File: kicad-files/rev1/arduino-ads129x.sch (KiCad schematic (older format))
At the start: 163 parts

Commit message: added 32kHz and 12MHz clock crystals
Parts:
- added C? (x4): 20pF, symbol C
- added X?: 12MHz 20pF, symbol CRYSTAL
- added X?: 32.768KHz 1.2pF, symbol CRYSTAL
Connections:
- wire segments 773 -> 608

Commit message: connected USB to SAM3X
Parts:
- added C?: 20pF, symbol C
- added R? (x2): 39, symbol R
- added R?: 6.8k, symbol R
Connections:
- wire segments 608 -> 814
- no-connect marks 1 -> 3
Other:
- note added: "See SAM3X data sheet section 40.5.1.9 Plug-In Detection:\nIn device mode, USB is detected when VBUS >= 1.4V"
- note added: "UOTGVBOF not needed; won't power VBUS\n"
- note added: "USB OTG ID not connected is slave"

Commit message: added fuse and zener on isolated side
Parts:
- added D?: ZENER, symbol ZENER
- added TH?: PTC, symbol THERMISTOR
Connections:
- wire segments 814 -> 624

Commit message: added power indicator LED to isolated 3.3V
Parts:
- added D?: LED, symbol LED
- added R?: 1k, symbol R
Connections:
- wire segments 624 -> 627
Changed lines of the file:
@@
-EESchema Schematic File Version 2  date Sat 18 May 2013 12:56:10 PM CEST
+EESchema Schematic File Version 2  date Sat 18 May 2013 01:12:58 PM CEST
 LIBS:power
 LIBS:device
@@
 $EndDescr
 Wire Wire Line
+	25700 4750 25700 4950
+Wire Wire Line
 	32850 2450 33000 2450
 Wire Wire Line
-	19250 16900 19250 17900
+	19250 17900 19250 16900
 Connection ~ 18950 17650
 Wire Wire Line
@@
 	20150 18450 20150 18400
 Wire Wire Line
-	20500 18450 20500 18500
+	20500 18500 20500 18450
 Connection ~ 20750 17700
 Connection ~ 17200 15900
@@
 	36150 5200 36050 5200
 Wire Wire Line
-	35600 4400 36150 4400
+	36150 4400 35600 4400
 Wire Wire Line
 	36150 4000 35950 4000
@@
 	33400 2450 33700 2450
 Wire Wire Line
-	35300 2450 35900 2450
+	35900 2450 35300 2450
 Wire Wire Line
 	34500 2600 34500 2450
@@
 	37300 1700 37300 750
 Wire Wire Line
-	38700 2450 39550 2450
+	39550 2450 38700 2450
 Connection ~ 39100 2450
 Connection ~ 35500 2450
@@
 	38800 2900 38800 3100
 Wire Wire Line
-	38100 2450 38000 2450
+	38000 2450 38100 2450
 Wire Wire Line
 	38000 3100 38000 2650
@@
 Connection ~ 18100 5450
 Wire Wire Line
-	20050 5450 18100 5450
-Wire Wire Line
-	18100 5550 18100 5400
+	18100 5450 20050 5450
+Wire Wire Line
+	18100 5400 18100 5550
 Connection ~ 17950 6600
 Wire Wire Line
@@
 Connection ~ 21300 7350
 Wire Wire Line
-	21650 7350 20900 7350
-Wire Wire Line
-	20900 7450 20900 7300
+	20900 7350 21650 7350
+Wire Wire Line
+	20900 7300 20900 7450
 Wire Wire Line
 	21300 7450 21300 7350
@@
 	20100 7350 20100 7450
 Wire Wire Line
-	18500 7450 18500 6600
+	18500 6600 18500 7450
 Connection ~ 16600 6100
 Wire Wire Line
@@
 Connection ~ 17000 5450
 Wire Wire Line
-	17350 5450 16600 5450
+	16600 5450 17350 5450
 Wire Wire Line
 	22000 4700 22000 4800
@@
 	22400 5550 22400 5450
 Wire Wire Line
-	22000 5550 22000 5400
-Wire Wire Line
-	20900 5550 20900 5400
+	22000 5400 22000 5550
+Wire Wire Line
+	20900 5400 20900 5550
 Wire Wire Line
 	21300 5550 21300 5450
@@
 	10900 1200 10900 2600
 Wire Wire Line
-	15250 2050 13950 2050
+	13950 2050 15250 2050
 Connection ~ 15350 800
 Wire Wire Line
@@
 	10800 1900 10800 2600
 Wire Wire Line
-	12550 4550 12550 5250
+	12550 5250 12550 4550
 Connection ~ 13950 800
 Wire Wire Line
@@
 	700  950  700  900
 Wire Wire Line
-	1250 1000 1250 850
-Wire Wire Line
-	1000 1000 1000 850
+	1250 850  1250 1000
+Wire Wire Line
+	1000 850  1000 1000
 Wire Wire Line
 	2950 4200 3000 4200
@@
 	5350 6950 5350 6750
 Wire Wire Line
-	5600 6750 5150 6750
+	5150 6750 5600 6750
 Wire Wire Line
 	5750 6950 5950 6950
@@
 	5950 6500 5750 6500
 Wire Wire Line
-	5600 6300 5150 6300
+	5150 6300 5600 6300
 Wire Wire Line
 	5350 6500 5350 6300
@@
 	5350 5600 5350 5400
 Wire Wire Line
-	5150 5400 5600 5400
+	5600 5400 5150 5400
 Wire Wire Line
 	5750 5600 5950 5600
@@
 	5950 6050 5750 6050
 Wire Wire Line
-	5150 5850 5600 5850
+	5600 5850 5150 5850
 Wire Wire Line
 	5350 6050 5350 5850
@@
 	5350 7850 5350 7650
 Wire Wire Line
-	5600 7650 5150 7650
+	5150 7650 5600 7650
 Wire Wire Line
 	5750 7850 5950 7850
@@
 	5950 7400 5750 7400
 Wire Wire Line
-	5600 7200 5150 7200
+	5150 7200 5600 7200
 Wire Wire Line
 	5350 7400 5350 7200
@@
 	5350 8300 5350 8100
 Wire Wire Line
-	5150 8100 5600 8100
+	5600 8100 5150 8100
 Wire Wire Line
 	5750 8300 5950 8300
@@
 	5950 8750 5750 8750
 Wire Wire Line
-	5150 8550 5600 8550
+	5600 8550 5150 8550
 Wire Wire Line
 	5350 8750 5350 8550
@@
 	5350 5150 5350 4950
 Wire Wire Line
-	5600 4950 5150 4950
+	5150 4950 5600 4950
 Wire Wire Line
 	5750 5150 5950 5150
@@
 	5950 4700 5750 4700
 Wire Wire Line
-	5600 4500 5150 4500
+	5150 4500 5600 4500
 Wire Wire Line
 	5350 4700 5350 4500
@@
 	5350 3800 5350 3600
 Wire Wire Line
-	5150 3600 5600 3600
+	5600 3600 5150 3600
 Wire Wire Line
 	5750 3800 5950 3800
@@
 	5950 4250 5750 4250
 Wire Wire Line
-	5150 4050 5600 4050
+	5600 4050 5150 4050
 Wire Wire Line
 	5350 4250 5350 4050
@@
 	5350 2450 5350 2250
 Wire Wire Line
-	5600 2250 5150 2250
+	5150 2250 5600 2250
 Wire Wire Line
 	5750 2450 5950 2450
@@
 	5950 2000 5750 2000
 Wire Wire Line
-	5600 1800 5150 1800
+	5150 1800 5600 1800
 Wire Wire Line
 	5350 2000 5350 1800
@@
 	5350 2900 5350 2700
 Wire Wire Line
-	5150 2700 5600 2700
+	5600 2700 5150 2700
 Wire Wire Line
 	5750 2900 5950 2900
@@
 	5950 3350 5750 3350
 Wire Wire Line
-	5150 3150 5600 3150
+	5600 3150 5150 3150
 Wire Wire Line
 	9600 4450 9500 4450
@@
 	2350 4350 2350 4300
 Wire Wire Line
-	1000 1150 1000 1400
-Wire Wire Line
-	1250 1150 1250 1400
+	1000 1400 1000 1150
+Wire Wire Line
+	1250 1400 1250 1150
 Wire Wire Line
 	1550 900  1550 950
@@
 Connection ~ 19300 5450
 Wire Wire Line
-	16600 5550 16600 5400
-Wire Wire Line
-	20900 5450 21750 5450
+	16600 5400 16600 5550
+Wire Wire Line
+	21750 5450 20900 5450
 Connection ~ 21300 5450
 Wire Wire Line
-	22000 5450 22750 5450
+	22750 5450 22000 5450
 Connection ~ 22400 5450
 Wire Wire Line
@@
 Connection ~ 18900 7350
 Wire Wire Line
-	18500 7350 20500 7350
+	20500 7350 18500 7350
 Connection ~ 18500 6600
 Wire Wire Line
@@
 	42900 2200 42900 2550
 Wire Wire Line
-	43250 3300 43250 2950
+	43250 2950 43250 3300
 Connection ~ 43250 3100
 Wire Wire Line
-	41950 2450 39750 2450
+	39750 2450 41950 2450
 Wire Wire Line
 	43250 2400 44000 2400
@@
 Connection ~ 26700 2450
 Wire Wire Line
-	26700 2500 26700 2400
+	26700 2400 26700 2500
 Connection ~ 27050 1850
 Wire Wire Line
@@
 Connection ~ 29200 2350
 Wire Wire Line
-	29750 2350 28550 2350
+	28550 2350 29750 2350
 Wire Wire Line
 	28850 2600 28850 2550
@@
 Connection ~ 26700 1850
 Wire Wire Line
-	26700 2450 27250 2450
+	27250 2450 26700 2450
 Wire Wire Line
 	27050 2350 27050 2450
@@
 Connection ~ 26700 5550
 Wire Wire Line
-	26250 4750 26250 5550
-Wire Wire Line
-	26250 5550 29750 5550
+	26250 5550 26250 4750
 Connection ~ 27050 4900
 Wire Wire Line
 	27050 4800 27050 4900
 Wire Wire Line
-	27250 4900 26700 4900
+	26700 4900 27250 4900
 Connection ~ 26700 4300
 Wire Wire Line
@@
 	28850 5000 28850 5050
 Wire Wire Line
-	28550 4800 29750 4800
+	29750 4800 28550 4800
 Connection ~ 29200 4800
 Wire Wire Line
@@
 Connection ~ 27050 4300
 Wire Wire Line
-	26700 4850 26700 4950
+	26700 4950 26700 4850
 Connection ~ 26700 4900
 Wire Wire Line
@@
 Connection ~ 41750 2450
 Wire Wire Line
-	38400 4400 39000 4400
+	39000 4400 38400 4400
 Wire Wire Line
 	38650 4800 38400 4800
@@
 Connection ~ 23350 5450
 Wire Wire Line
-	23700 5450 22950 5450
-Wire Wire Line
-	22950 5550 22950 5400
+	22950 5450 23700 5450
+Wire Wire Line
+	22950 5400 22950 5550
 Wire Wire Line
 	23350 5550 23350 5450
@@
 Connection ~ 16950 16650
 Wire Wire Line
-	20150 18000 20150 16250
+	20150 16250 20150 18000
 Wire Wire Line
 	19400 16400 19400 16250
@@
 Connection ~ 19400 17150
 Wire Wire Line
-	18950 18400 18950 18150
+	18950 18150 18950 18400
 Wire Wire Line
 	18700 18200 18700 18250
@@
 Connection ~ 18950 18250
 Wire Wire Line
-	19400 16900 19400 17900
-Wire Wire Line
-	18950 17750 18950 16250
+	19400 17900 19400 16900
+Wire Wire Line
+	18950 16250 18950 17750
 Wire Wire Line
 	33700 2850 31550 2850
 Connection ~ 32200 2850
 Wire Wire Line
-	32350 2450 31550 2450
+	31550 2450 32350 2450
 Connection ~ 32200 2450
+Wire Wire Line
+	25700 4300 25700 4350
+Connection ~ 25700 4300
+Wire Wire Line
+	25700 5450 25700 5550
+Wire Wire Line
+	25700 5550 29750 5550
+Connection ~ 26250 5550
+$Comp
+L R R?
+U 1 1 51976086
+P 25700 5200
+F 0 "R?" V 25780 5200 50  0000 C CNN
+F 1 "1k" V 25700 5200 50  0000 C CNN
+	1    25700 5200
+	1    0    0    -1
+$EndComp
+$Comp
+L LED D?
+U 1 1 51976061
+P 25700 4550
+F 0 "D?" H 25700 4650 50  0000 C CNN
+F 1 "LED" H 25700 4450 50  0000 C CNN
+	1    25700 4550
+	0    1    1    0
+$EndComp
 $Comp
 L ZENER D?

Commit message: added reset button
A capacitor is not strictly required, but the data sheet
recommends a 10nF capacitor in harsh environments.

We chose a 100nF capacitor to keep the parts list and
assembly instructions simple.
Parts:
- added C?: 100nF, symbol C
- added SW?: SW_PUSH, symbol SW_PUSH
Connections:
- net labels added: RESET
- wire segments 627 -> 633
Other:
- note added: "Data sheet\nspec is\n10nF"

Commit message: added JTAG
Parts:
- added P?: JTAG, symbol CONN_5X2
- added R? (x4): 100k, symbol R
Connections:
- net labels added: JTAG_RESET, JTAG_TCK, JTAG_TDI, JTAG_TDO, JTAG_TMS
- wire segments 633 -> 659
- no-connect marks 3 -> 4

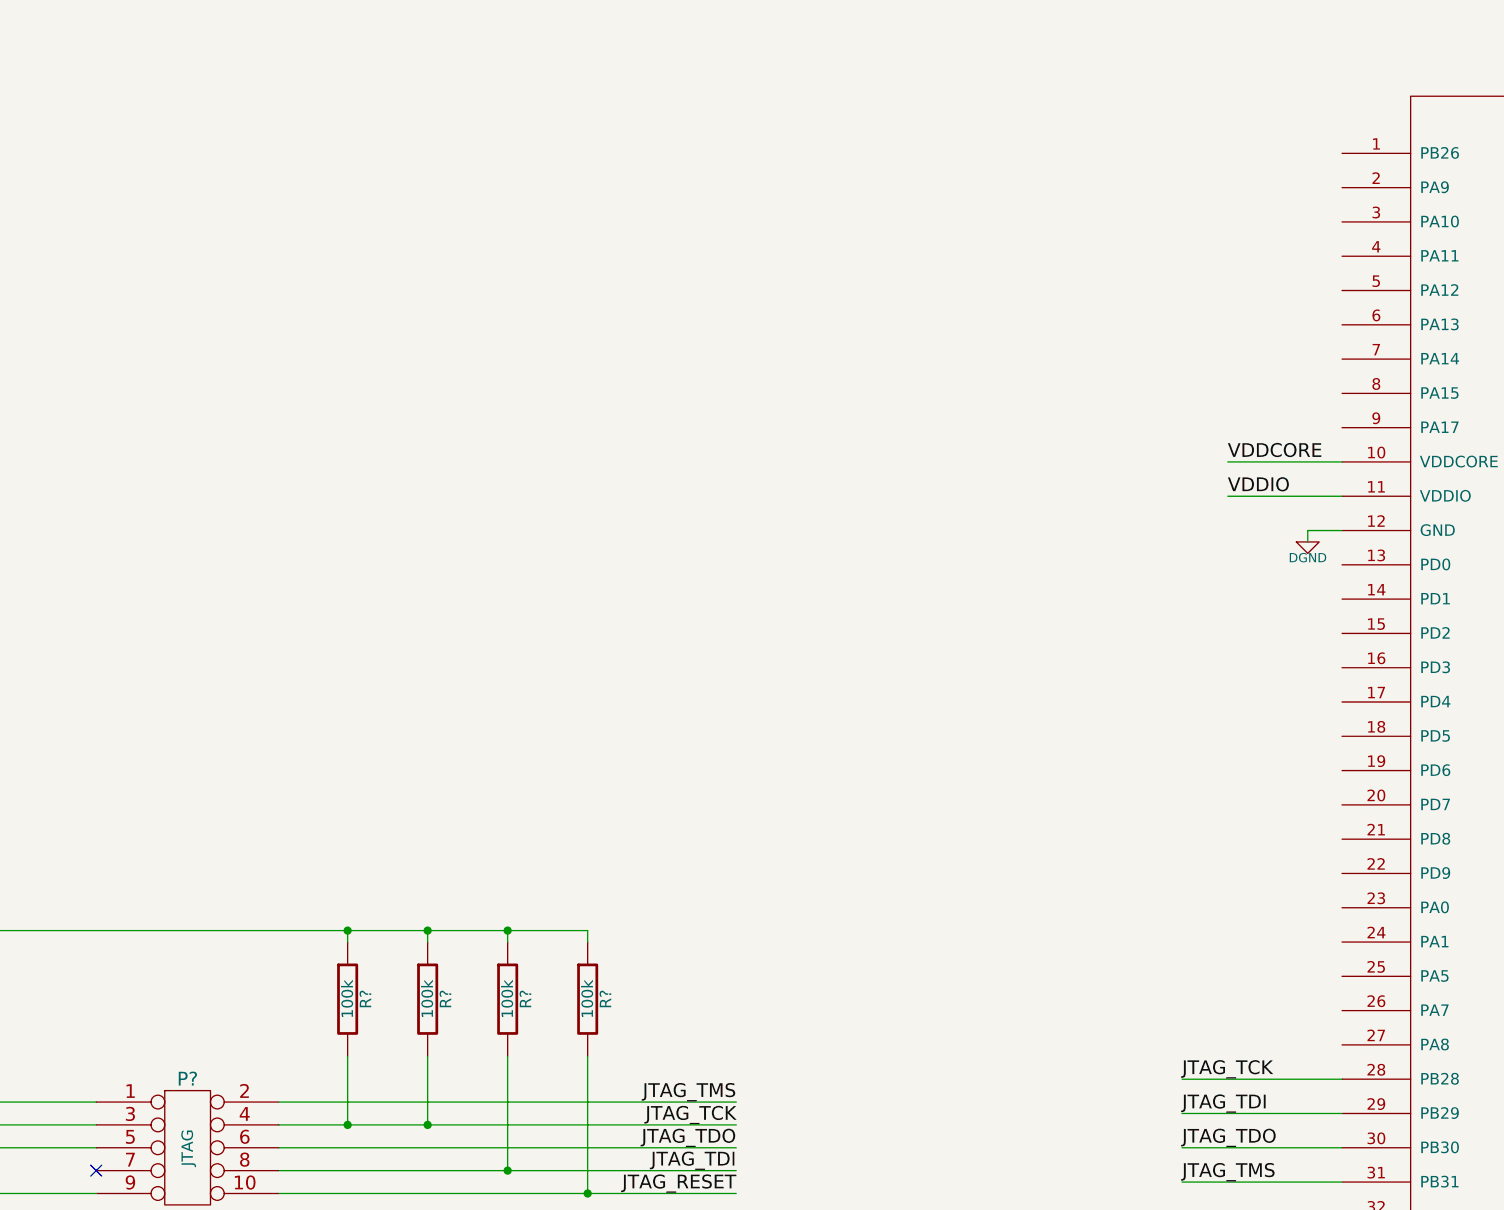
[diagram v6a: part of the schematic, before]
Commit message: added serial header for programming port
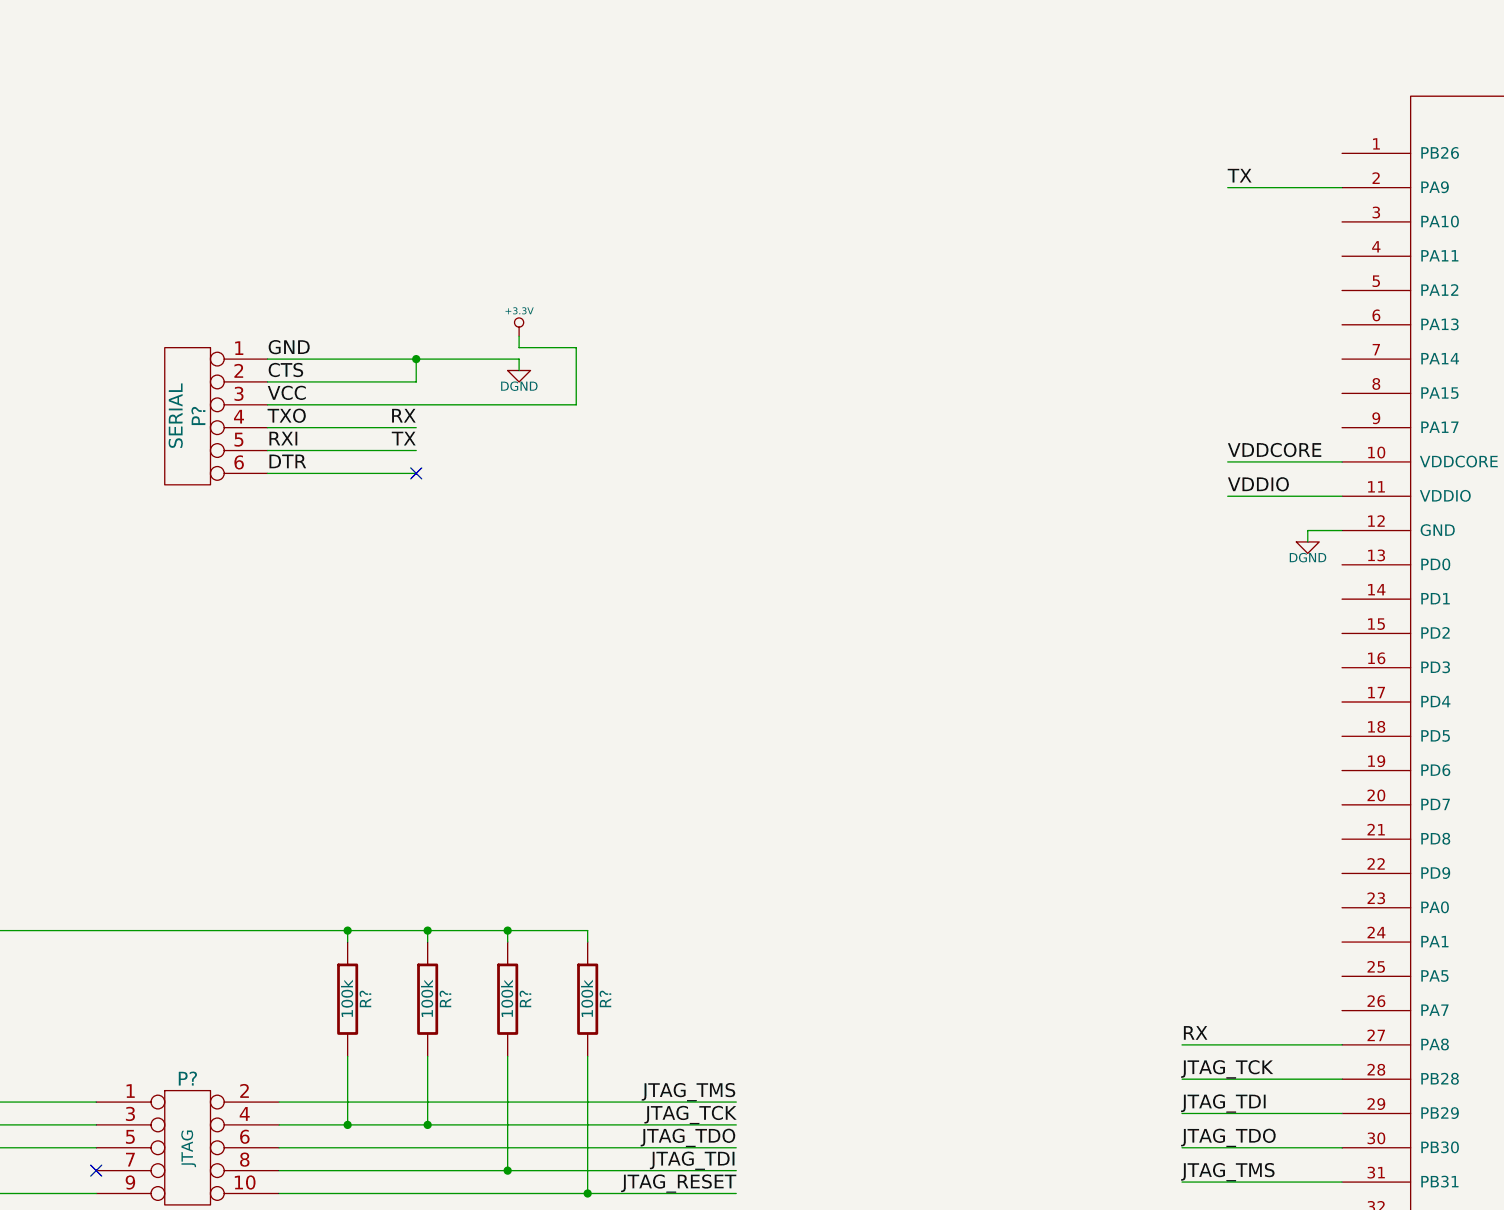
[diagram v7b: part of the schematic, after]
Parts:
- added P?: SERIAL, symbol CONN_6
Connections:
- net labels added: CTS, DTR, RX, RXI, TX, TXO, VCC
- wire segments 659 -> 672
- no-connect marks 4 -> 5
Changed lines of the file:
@@
-EESchema Schematic File Version 2  date Sat 18 May 2013 02:24:49 PM CEST
+EESchema Schematic File Version 2  date Sat 18 May 2013 03:01:05 PM CEST
 LIBS:power
 LIBS:device
@@
 Comment4 ""
 $EndDescr
-Text Label 17000 15050 0    60   ~ 0
-JTAG_TMS
+Connection ~ 13650 11450
+Wire Wire Line
+	13650 11450 13650 11550
+Wire Wire Line
+	14100 11500 14100 11450
+Wire Wire Line
+	13000 11950 13650 11950
+Wire Wire Line
+	13000 11750 13650 11750
+Wire Wire Line
+	13650 11550 13000 11550
+Wire Wire Line
+	17700 14450 17000 14450
 Wire Wire Line
 	17700 15050 17000 15050
@@
 Wire Wire Line
 	17700 14900 17000 14900
+Wire Wire Line
+	17700 10700 17200 10700
+Wire Wire Line
+	13000 11850 13650 11850
+Wire Wire Line
+	13000 11650 14350 11650
+Wire Wire Line
+	14350 11650 14350 11400
+Wire Wire Line
+	14350 11400 14100 11400
+Wire Wire Line
+	14100 11400 14100 11350
+Wire Wire Line
+	14100 11450 13000 11450
+$Comp
+L DGND #PWR?
+U 1 1 51977B33
+P 14100 11500
+F 0 "#PWR?" H 14100 11500 40  0001 C CNN
+F 1 "DGND" H 14100 11430 40  0000 C CNN
+	1    14100 11500
+	1    0    0    -1
+$EndComp
+$Comp
+L +3.3V #PWR?
+U 1 1 51977B17
+P 14100 11350
+F 0 "#PWR?" H 14100 11310 30  0001 C CNN
+F 1 "+3.3V" H 14100 11460 30  0000 C CNN
+	1    14100 11350
+	1    0    0    -1
+$EndComp
+Text Label 13650 11850 2    60   ~ 0
+TX
+Text Label 13650 11750 2    60   ~ 0
+RX
+NoConn ~ 13650 11950
+Text Label 13000 11950 0    60   ~ 0
+DTR
+Text Label 13000 11850 0    60   ~ 0
+RXI
+Text Label 13000 11750 0    60   ~ 0
+TXO
+Text Label 13000 11650 0    60   ~ 0
+VCC
+Text Label 13000 11550 0    60   ~ 0
+CTS
+Text Label 13000 11450 0    60   ~ 0
+GND
+Text Label 17000 14450 0    60   ~ 0
+RX
+Text Label 17200 10700 0    60   ~ 0
+TX
+$Comp
+L CONN_6 P?
+U 1 1 5197789B
+P 12650 11700
+F 0 "P?" V 12600 11700 60  0000 C CNN
+F 1 "SERIAL" V 12700 11700 60  0000 C CNN
+	1    12650 11700
+	-1   0    0    -1
+$EndComp
+Text Label 17000 15050 0    60   ~ 0
+JTAG_TMS
 Text Label 17000 14900 0    60   ~ 0
 JTAG_TDO

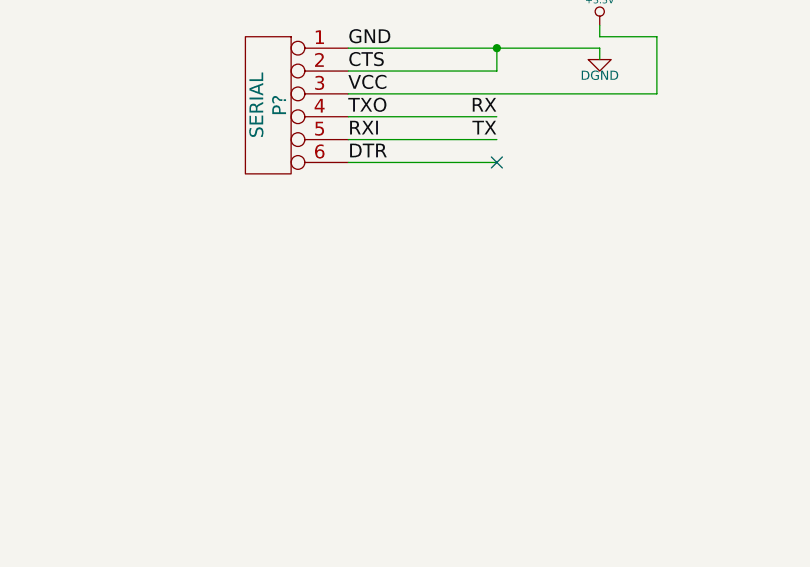
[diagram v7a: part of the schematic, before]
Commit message: added serial header for JY-MCU HC-06 bluetooth module
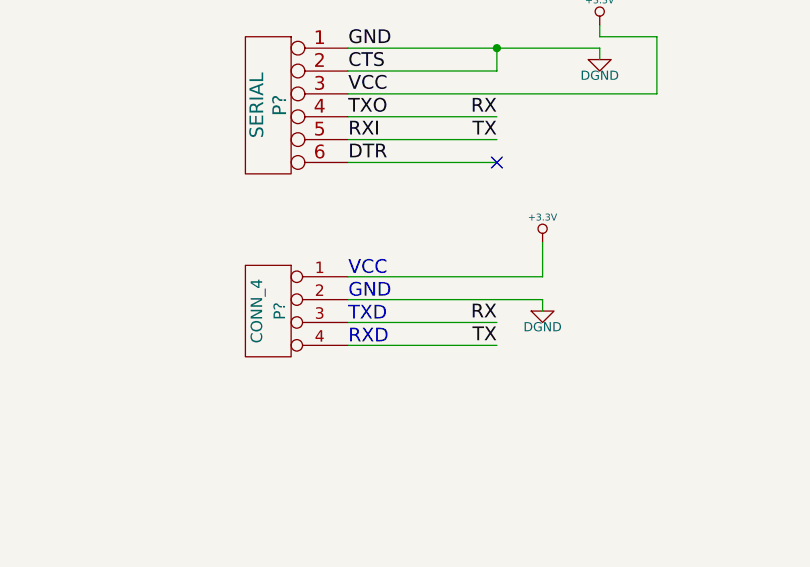
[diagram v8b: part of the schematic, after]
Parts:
- added P?: CONN_4, symbol CONN_4
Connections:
- wire segments 672 -> 678
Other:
- note added: "GND"
- note added: "RXD"
- note added: "TXD"
- note added: "VCC"
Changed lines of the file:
@@
-EESchema Schematic File Version 2  date Sat 18 May 2013 03:01:05 PM CEST
+EESchema Schematic File Version 2  date Sat 18 May 2013 03:09:57 PM CEST
 LIBS:power
 LIBS:device
@@
 Comment4 ""
 $EndDescr
+Text Label 13650 12750 2    60   ~ 0
+TX
+Text Label 13650 12650 2    60   ~ 0
+RX
+Wire Wire Line
+	13850 12450 13850 12300
+Wire Wire Line
+	13000 12450 13850 12450
+Wire Wire Line
+	13850 12600 13850 12550
+Wire Wire Line
+	13000 12750 13650 12750
 Connection ~ 13650 11450
 Wire Wire Line
@@
 Wire Wire Line
 	14100 11450 13000 11450
+Wire Wire Line
+	13000 12650 13650 12650
+Wire Wire Line
+	13850 12550 13000 12550
+$Comp
+L DGND #PWR?
+U 1 1 51977D41
+P 13850 12600
+F 0 "#PWR?" H 13850 12600 40  0001 C CNN
+F 1 "DGND" H 13850 12530 40  0000 C CNN
+	1    13850 12600
+	1    0    0    -1
+$EndComp
+$Comp
+L +3.3V #PWR?
+U 1 1 51977D37
+P 13850 12300
+F 0 "#PWR?" H 13850 12260 30  0001 C CNN
+F 1 "+3.3V" H 13850 12410 30  0000 C CNN
+	1    13850 12300
+	1    0    0    -1
+$EndComp
+Text Notes 13000 12750 0    60   ~ 0
+RXD
+Text Notes 13000 12650 0    60   ~ 0
+TXD
+Text Notes 13000 12550 0    60   ~ 0
+GND
+Text Notes 13000 12450 0    60   ~ 0
+VCC
+Text Label 13000 11450 0    60   ~ 0
+GND
+$Comp
+L CONN_4 P?
+U 1 1 51977BF4
+P 12650 12600
+F 0 "P?" V 12600 12600 50  0000 C CNN
+F 1 "CONN_4" V 12700 12600 50  0000 C CNN
+	1    12650 12600
+	-1   0    0    -1
+$EndComp
 $Comp
 L DGND #PWR?
@@
 Text Label 13000 11550 0    60   ~ 0
 CTS
-Text Label 13000 11450 0    60   ~ 0
-GND
 Text Label 17000 14450 0    60   ~ 0
 RX
